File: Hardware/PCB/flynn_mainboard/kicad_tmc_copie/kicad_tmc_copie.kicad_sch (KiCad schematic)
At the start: 25 parts, among them J1 Conn_01x04, J2 Conn_01x02, SW1 SW_DIP_x02, U2 AZ1117-3.3

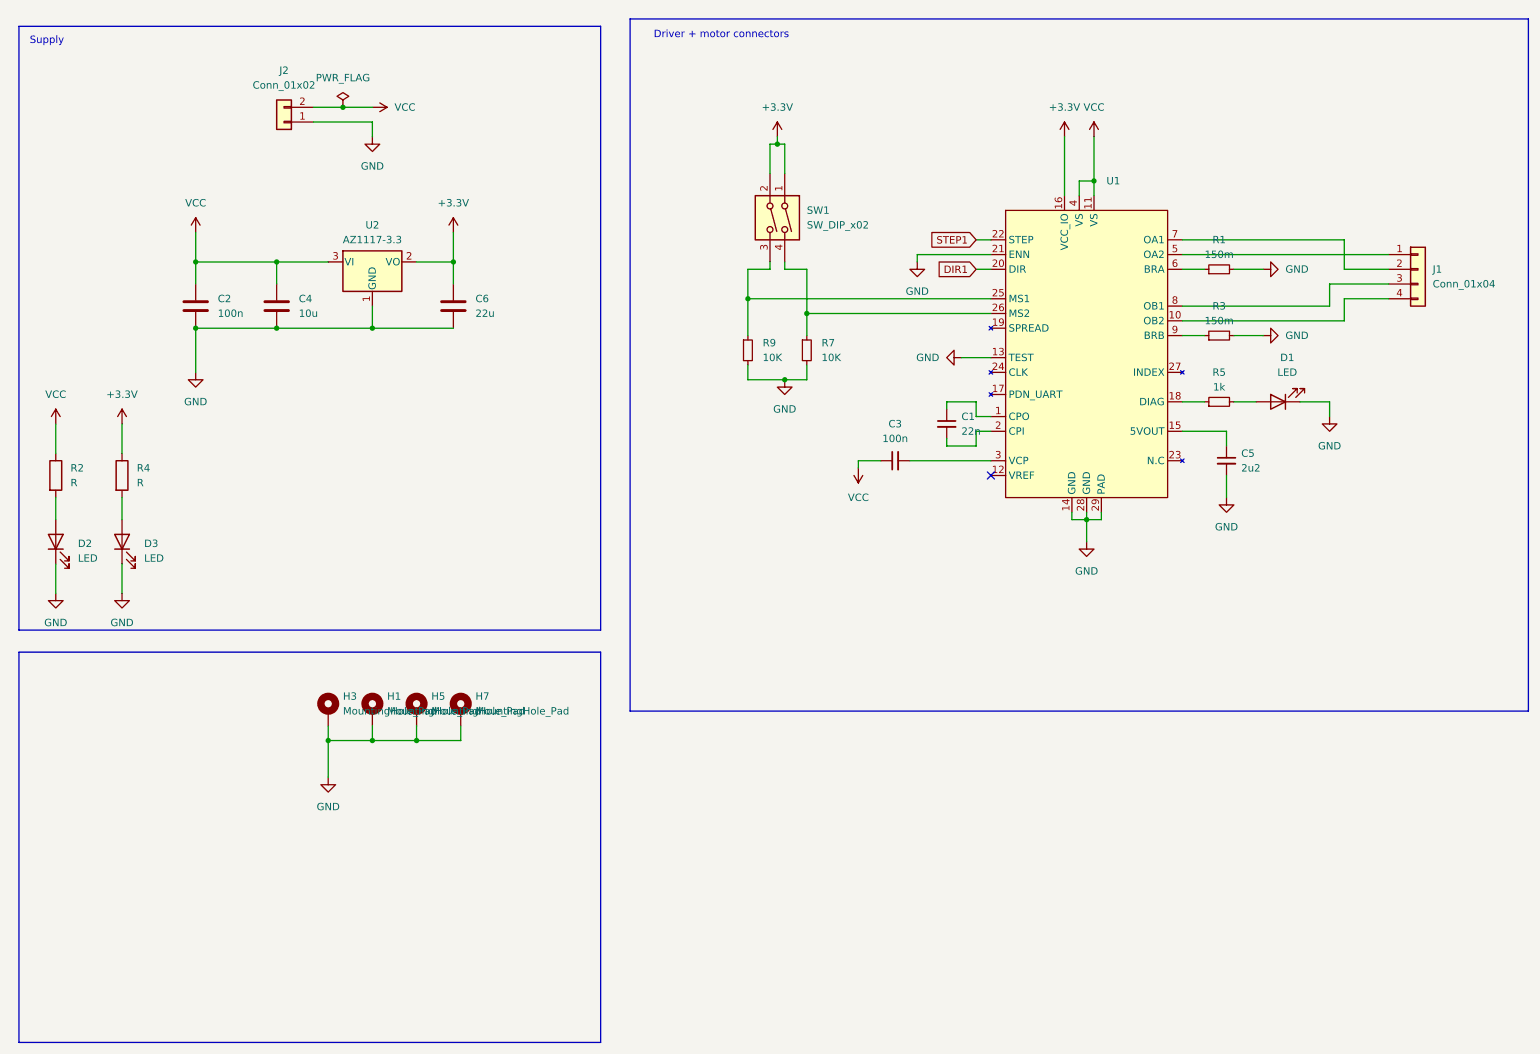
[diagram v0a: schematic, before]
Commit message: Ajout du schéma
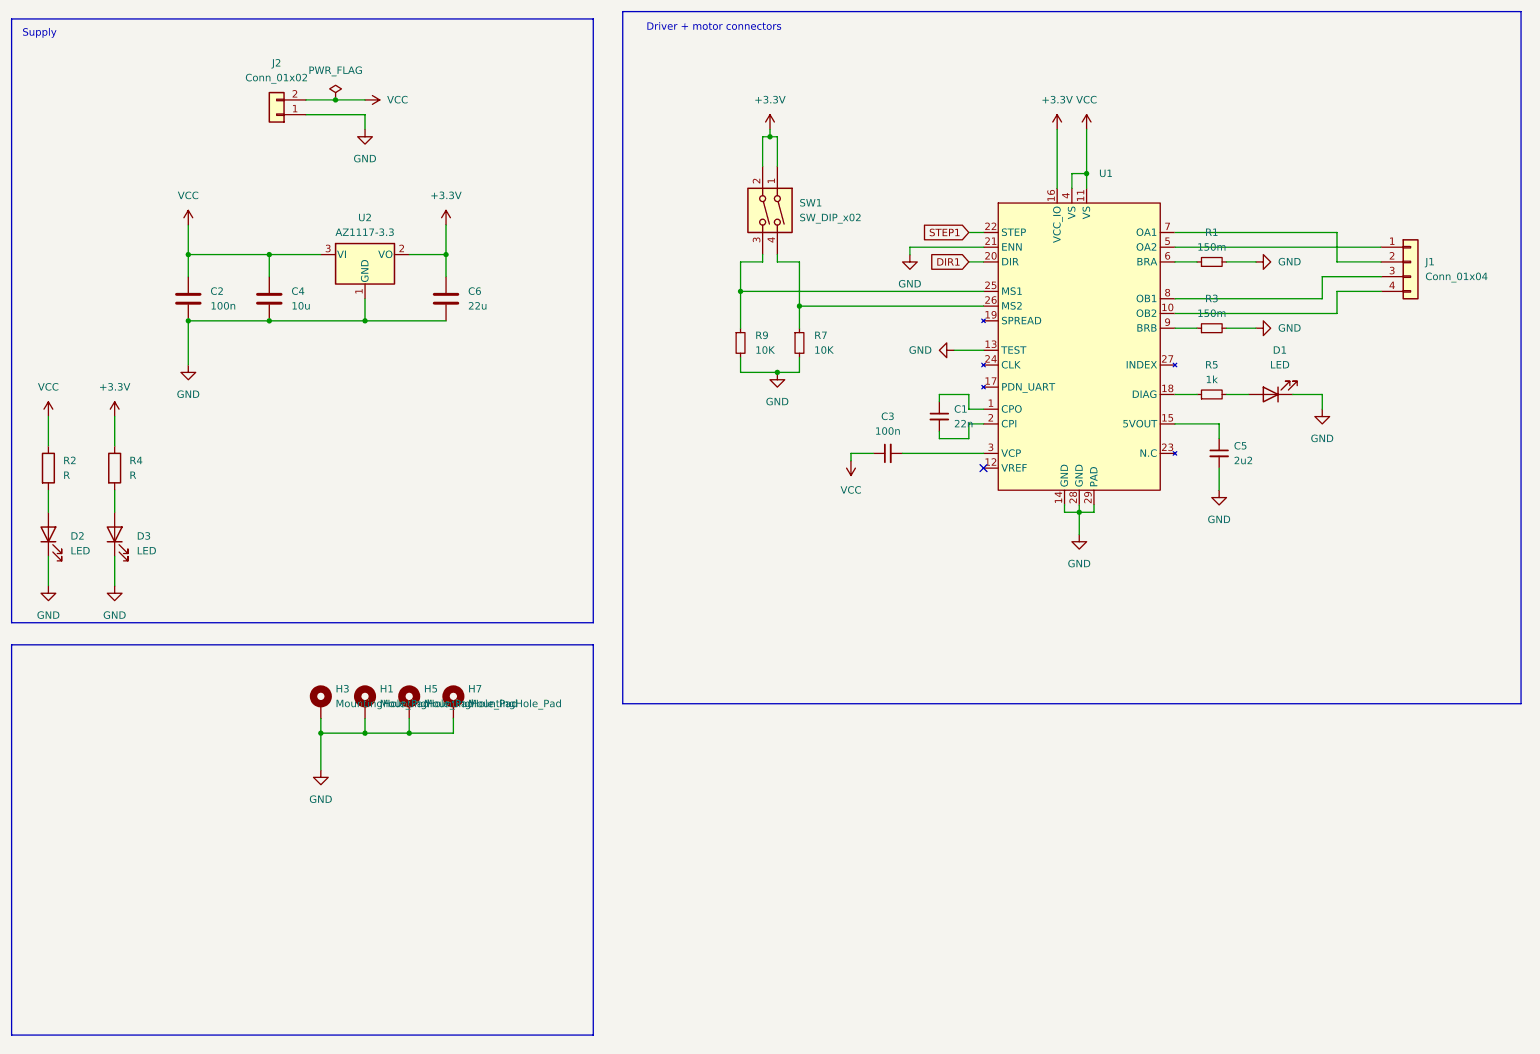
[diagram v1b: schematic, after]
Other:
- title: Flynn -> (none)
- moved on the sheet: C1, C2, C3, C4, C5, C6, D1, D2, D3, H1, H3, H5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
